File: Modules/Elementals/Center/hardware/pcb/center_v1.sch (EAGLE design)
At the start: 24 parts, among them J1 WQP-PJ398SM6, J10 WQP-PJ398SM6, J11 WQP-PJ398SM6, J12 WQP-PJ398SM6, J2 WQP-PJ398SM6, J3 WQP-PJ398SM6, J4 WQP-PJ398SM6, J5 WQP-PJ398SM6, J6 WQP-PJ398SM6, J7 WQP-PJ398SM6, J8 WQP-PJ398SM6, J9 WQP-PJ398SM6

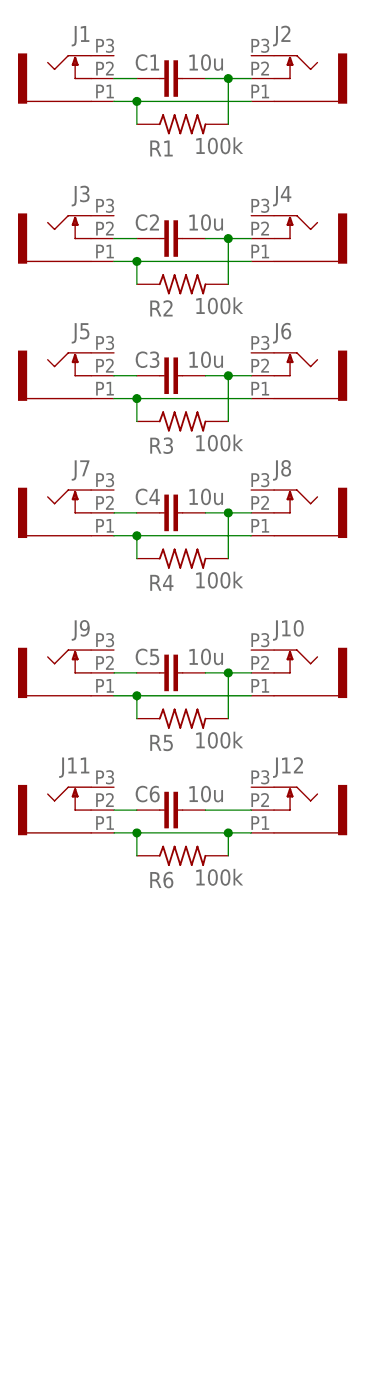
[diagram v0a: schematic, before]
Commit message: Finished center pcb and panel
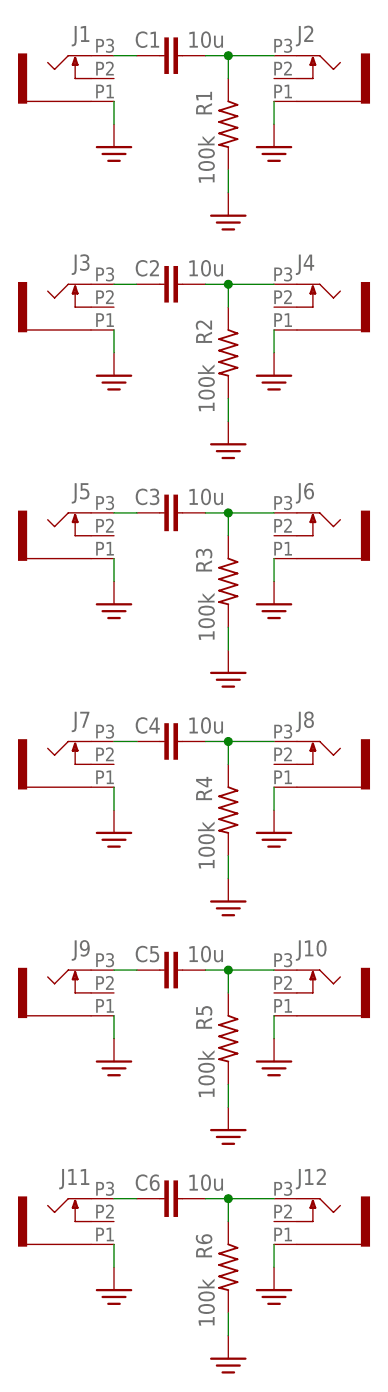
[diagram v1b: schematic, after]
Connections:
- removed net N$13: C5.1, J9.2
- removed net N$14: C5.2, J10.2, R5.2
- removed net N$15: J10.1, J9.1, R5.1
- removed net N$16: C6.1, J11.2
- removed net N$17: C6.2, J12.2
- removed net N$18: J11.1, J12.1, R6.1, R6.2
- new net GND: J1.1, J10.1, J11.1, J12.1, J2.1, J3.1, J4.1, J5.1, J6.1, J7.1, J8.1, J9.1, R1.2, R2.2, R3.2, R4.2, R5.2, R6.2
- net N$1: now also J1.3; no longer J1.2
- net N$10: now also C5.2, J10.3, R5.1; no longer C4.1, J7.2
- net N$11: now also C6.2, J12.3, R6.1; no longer C4.2, J8.2, R4.2
- net N$12: now also C6.1, J11.3; no longer J7.1, J8.1, R4.1
- net N$2: now also J2.3, R1.1; no longer J2.2, R1.2
- net N$3: now also C2.2, J4.3, R2.1; no longer J1.1, J2.1, R1.1
- net N$4: now also J3.3; no longer J3.2
- net N$5: now also C3.2, J6.3, R3.1; no longer C2.2, J4.2, R2.2
- net N$6: now also C3.1, J5.3; no longer J3.1, J4.1, R2.1
- net N$7: now also C4.1, J7.3; no longer C3.1, J5.2
- net N$8: now also C4.2, J8.3, R4.1; no longer C3.2, J6.2, R3.2
- net N$9: now also C5.1, J9.3; no longer J5.1, J6.1, R3.1
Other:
- moved on the sheet: C1, C2, C3, C4, C5, C6, J10, J11, J12, J2, J3, J4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
